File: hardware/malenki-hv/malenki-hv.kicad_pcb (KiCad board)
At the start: 4 copper layers, 19 x 32 mm, 49 parts, among them J1 Conn_01x02_Male-Connector, J2 Conn_01x08_Male, J3 Conn_01x02, J4 Conn_01x02_Male-Connector, J5 Conn_01x02_Male-Connector, J6 Conn_01x02_Male-Connector, U1 A7105, U2 AP2204RA-3.3TRG1, U3 ATTiny1616-MNR, U4 DRV8231DSGR, U5 DRV8231DSGR, U6 DRV8231DSGR, Y1 16mhz Seiko Epson Q24FA20H005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

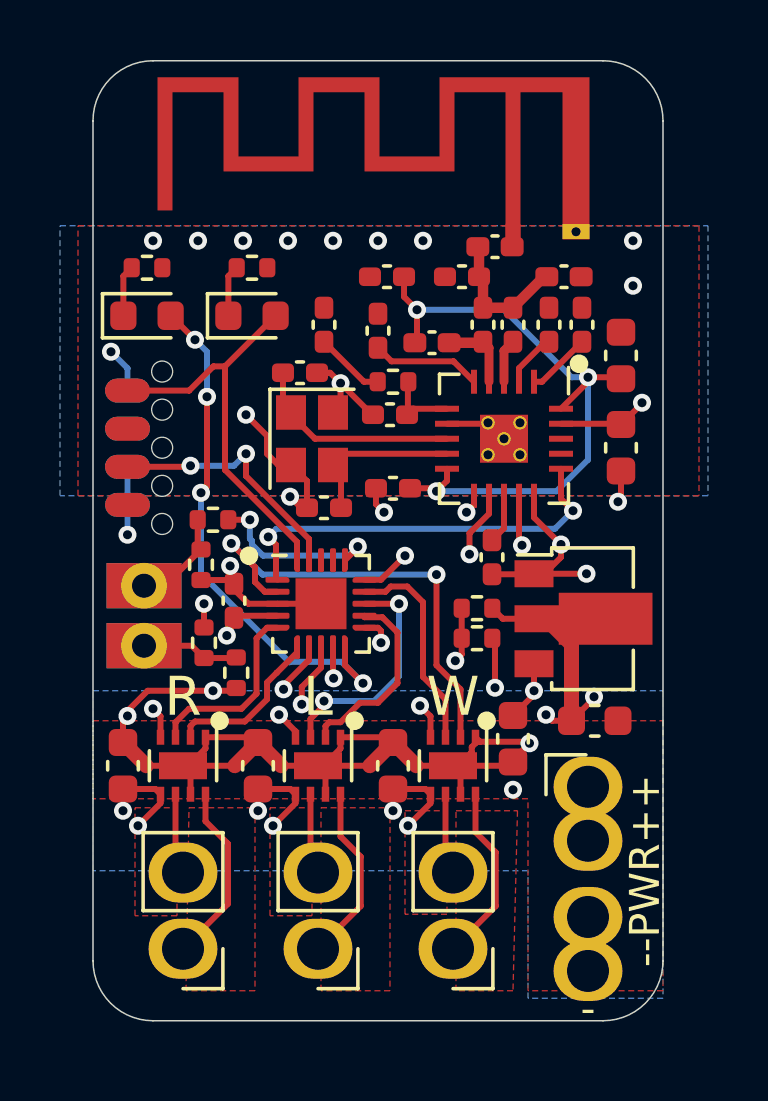
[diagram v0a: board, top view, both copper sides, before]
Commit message: Updated u1 QFN symbol by adding solder paste layer, minor schematic updates to fix check errors, converted to kiCad 9, Updated BOM with LSCS numbers, fixed BOM errors.
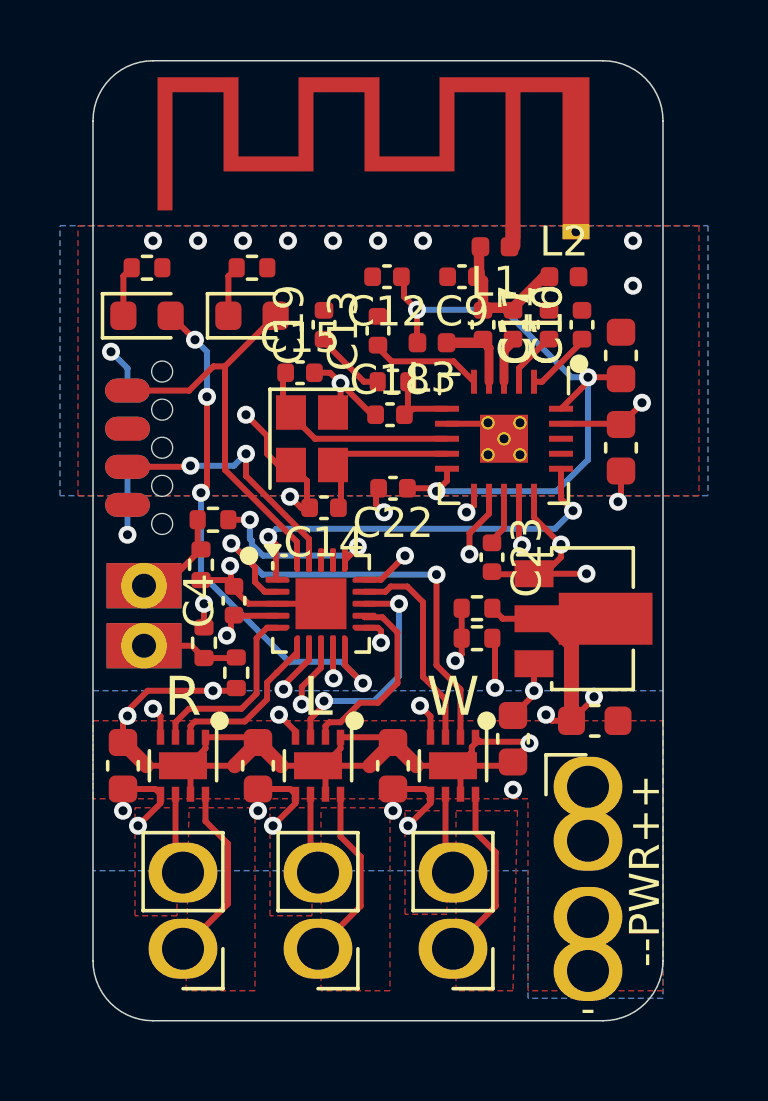
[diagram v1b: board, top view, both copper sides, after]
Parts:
- C10, C11, C12, C13, C14, C15, C16, C17, C18, C19, C22, C23, C4, C9: footprint Capacitor_SMD:C_0402_1005Metric_Pad0.74x0.62mm_HandSolder -> Capacitor_SMD:C_0402_1005Metric
- L1: value 2.7nH -> 2.7 nH; footprint Inductor_SMD:L_0402_1005Metric_Pad0.77x0.64mm_HandSolder -> Inductor_SMD:L_0402_1005Metric
- L2, L3: footprint Inductor_SMD:L_0402_1005Metric_Pad0.77x0.64mm_HandSolder -> Inductor_SMD:L_0402_1005Metric
- R1, R5, R6: value 470R -> 470Ω
- R2: value 1k -> 1kΩ
- R25: value 200R -> 200Ω
- R3: value 100k -> 100kΩ
- R4, R7, R8: value 10k -> 10kΩ
- U2: value AP2204RA-3.3TRG1 -> 300mA Fixed 3.3V Positive 24V SOT-89 Voltage Regulators - Linear, Low Drop Out (LDO) Regulators
- Y1: value 16mhz Seiko Epson Q24FA20H0051200 -> 16mhz Seiko Epson Q24FA20H0051200
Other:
- board text added: "Thank You For Supporting Noosa Robotics"
- board text removed: "@markxr 2023"

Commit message: Add F.Paste layer to U1, A7105
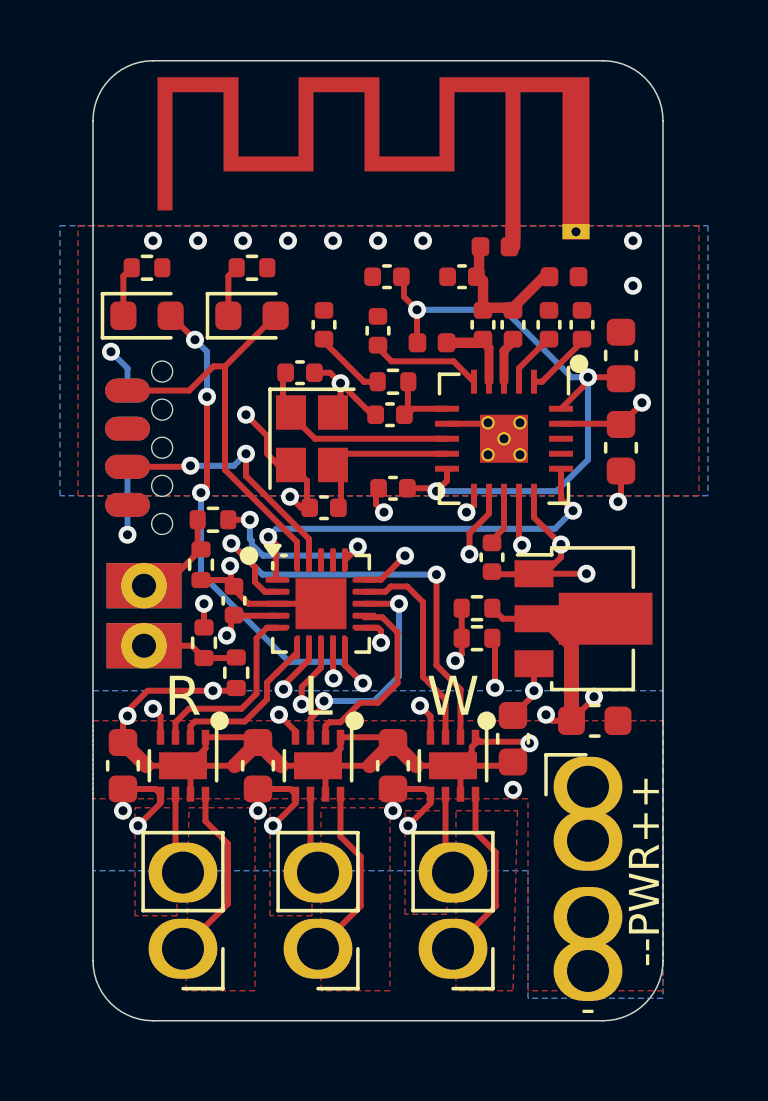
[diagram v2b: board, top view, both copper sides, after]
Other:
- board text added: "Designed By: Mark Robson"
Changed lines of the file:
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@@
 			(at 0 -1.16 180)
 			(layer "F.SilkS")
+			(hide yes)
 			(effects
 				(font
@@
 			(at 0 -1.16 0)
 			(layer "F.SilkS")
+			(hide yes)
 			(effects
 				(font
@@
 			(at 0 -1.17 180)
 			(layer "F.SilkS")
+			(hide yes)
 			(effects
 				(font
@@
 			(at 0 -1.16 90)
 			(layer "F.SilkS")
+			(hide yes)
 			(effects
 				(font
@@
 			(at 0 -1.16 90)
 			(layer "F.SilkS")
+			(hide yes)
 			(effects
 				(font
@@
 			(at 0 -1.17 0)
 			(layer "F.SilkS")
+			(hide yes)
 			(effects
 				(font
@@
 			(at 0 -1.16 270)
 			(layer "F.SilkS")
+			(hide yes)
 			(effects
 				(font
@@
 			(at 0 -1.16 90)
 			(layer "F.SilkS")
+			(hide yes)
 			(effects
 				(font
@@
 			(at 0 -1.17 180)
 			(layer "F.SilkS")
+			(hide yes)
 			(effects
 				(font
@@
 			(at 0 -1.16 180)
 			(layer "F.SilkS")
+			(hide yes)
 			(effects
 				(font
@@
 			(at 0 -1.16 90)
 			(layer "F.SilkS")
+			(hide yes)
 			(effects
 				(font
@@
 			(at 0 -1.16 180)
 			(layer "F.SilkS")
+			(hide yes)
 			(effects
 				(font
@@
 			(at 0 -1.16 270)
 			(layer "F.SilkS")
+			(hide yes)
 			(effects
 				(font
@@
 			(at 0 -1.16 270)
 			(layer "F.SilkS")
+			(hide yes)
 			(effects
 				(font
@@
 			(at 0 -1.16 0)
 			(layer "F.SilkS")
+			(hide yes)
 			(effects
 				(font
@@
 			(at 0 -1.16 180)
 			(layer "F.SilkS")
+			(hide yes)
 			(effects
 				(font
@@
 			(at 0 -1.16 90)
 			(layer "F.SilkS")
+			(hide yes)
 			(effects
 				(font
@@
 		)
 	)
+	(gr_text "Designed By:\nMark Robson"
+		(at 97.3 56.9 0)
+		(layer "B.SilkS")
+		(effects
+			(font
+				(size 1 1)
+				(thickness 0.15)
+			)
+			(justify mirror)
+		)
+	)
 	(gr_text "-"
 		(at 104.5 81.1 0)
@@
 	)
 	(gr_text "Thank You\nFor Supporting\nNoosa Robotics"
-		(at 97.5 58.5 0)
+		(at 94.3 65.4 270)
 		(layer "B.SilkS")
 		(effects
